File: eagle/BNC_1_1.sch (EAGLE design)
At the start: 14 parts, among them X1 In, X2 Mode, X3 Ctrl, X4 Out, X5 Out C/B

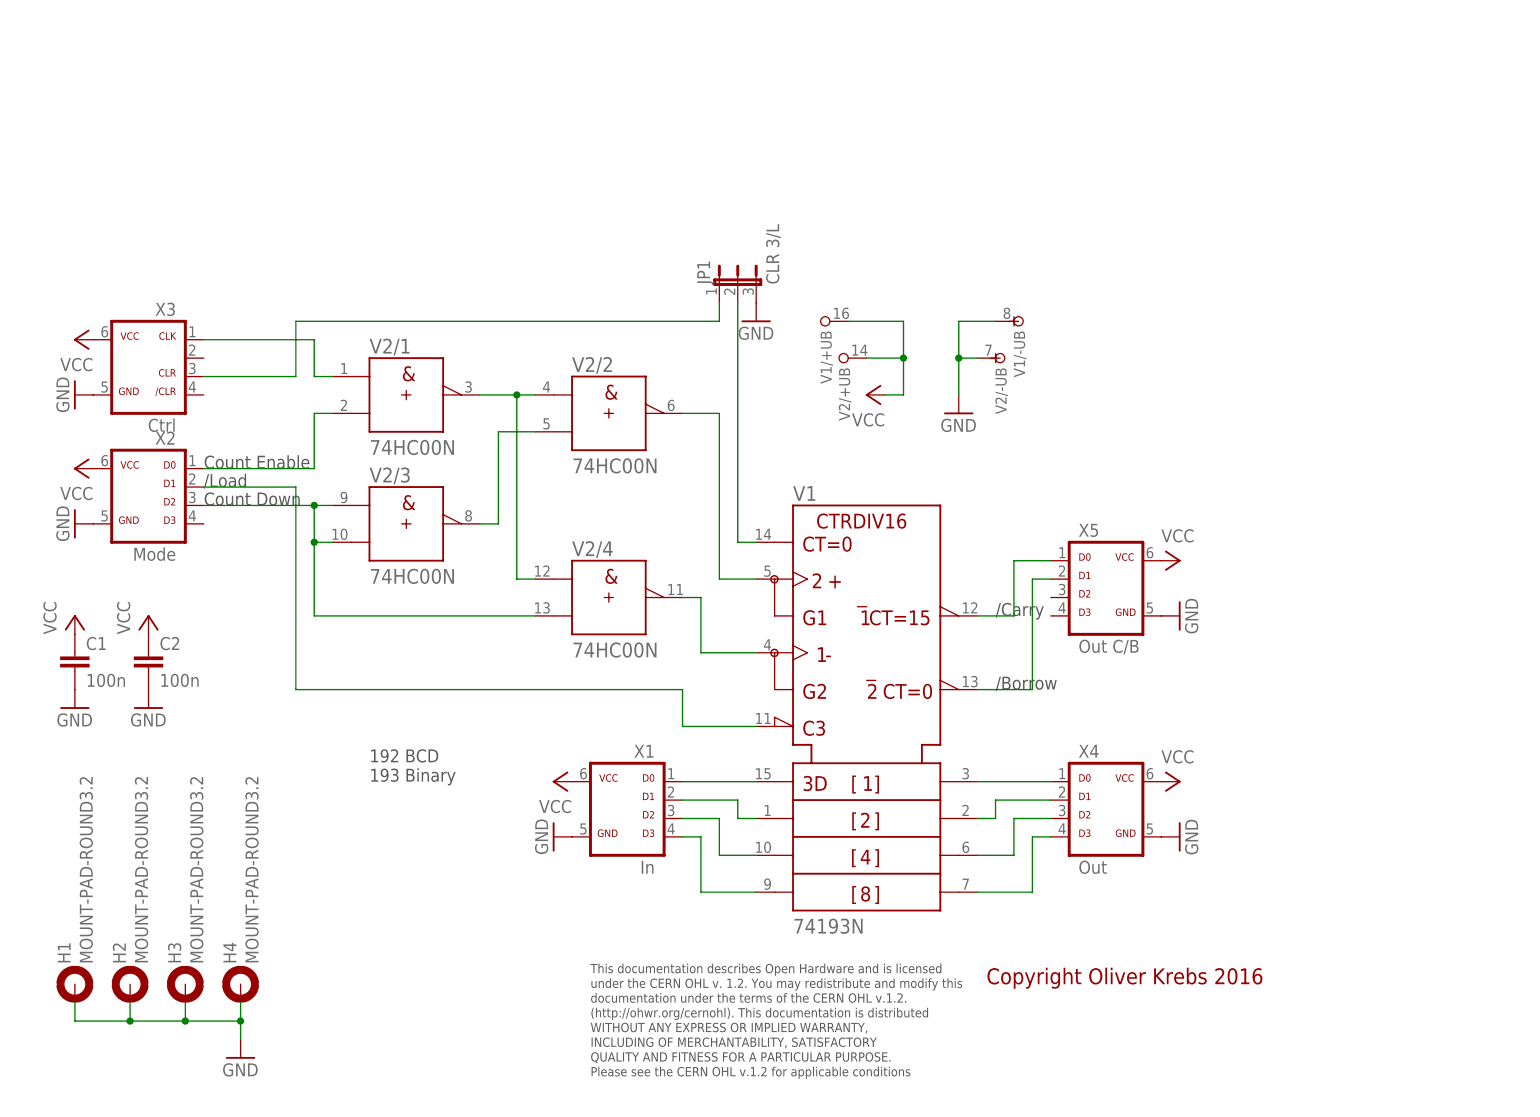
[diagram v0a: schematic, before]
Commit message: Add new tetra-Board and arduino files
Add AMP_1_0, AVC_1_0, D18_1_1, IOP_1_2, MIC_1_0, PIN_1_1, POT_1_0, PWA_1_0, PWR_1_0, RGF 2.0, SOC_2_0, VLT_1_0
Add mex_nano_shield_keyboard, mex_nano_shied_numbers

New arduino projects
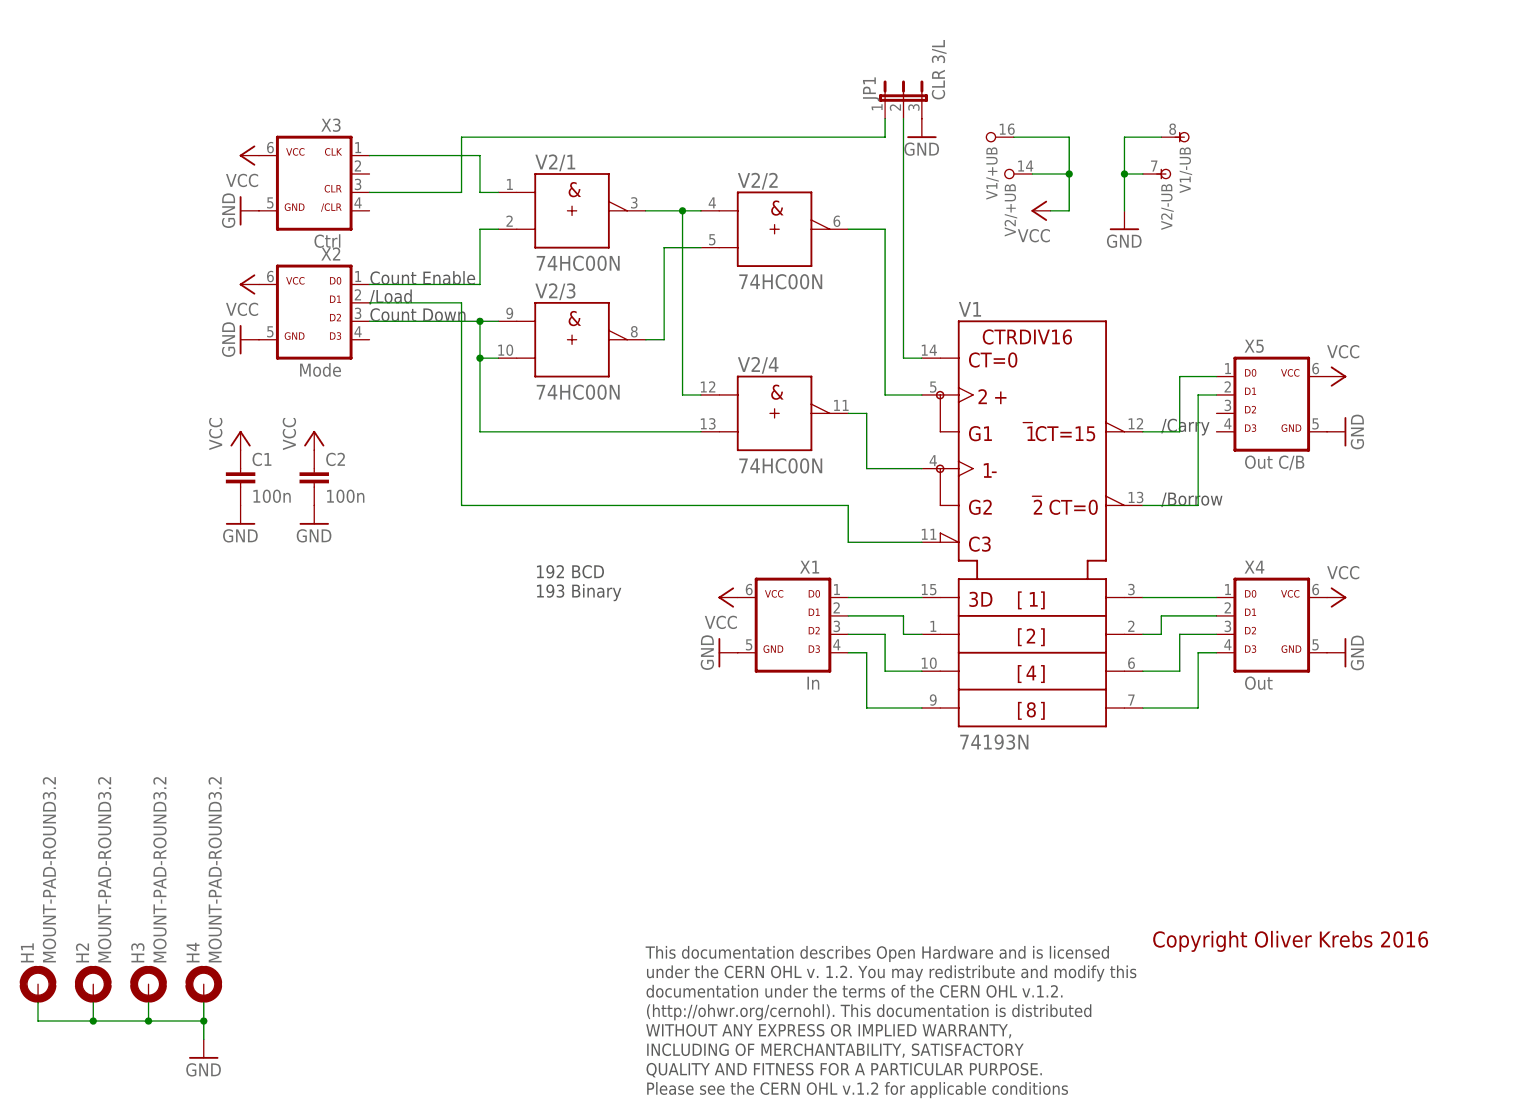
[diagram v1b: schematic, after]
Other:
- moved on the sheet: C1, C2, H1, H2, H3, H4, JP1, V1, V1/+UB, V1/-UB, V2/+UB, V2/-UB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
